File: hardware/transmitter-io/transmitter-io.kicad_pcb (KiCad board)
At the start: 2 copper layers, 68.6 x 53.3 mm, 20 parts, among them J1 Input

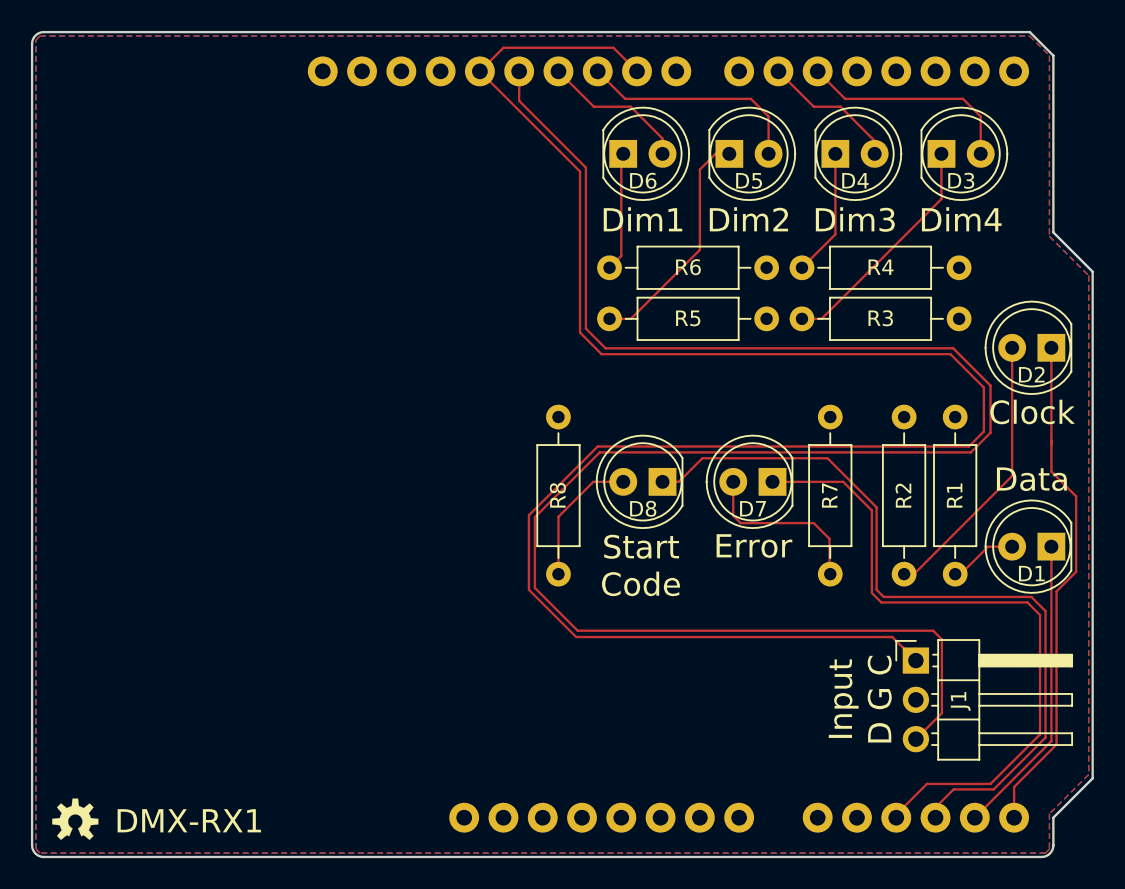
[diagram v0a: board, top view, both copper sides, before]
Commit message: Prototype version of DMX, Analog, and PWM IO Modules and both TX and RX IO interfaces.
Make io-analog a stackable family
io-analog-core handles D to A
io-analog-voltage handles voltage output
io-analog-pwm handles pwm output for leds, drive display pro

Refactor display-pro to work with io-analog-pwm
Add correct coax power connector

Move TX2 to tx-io
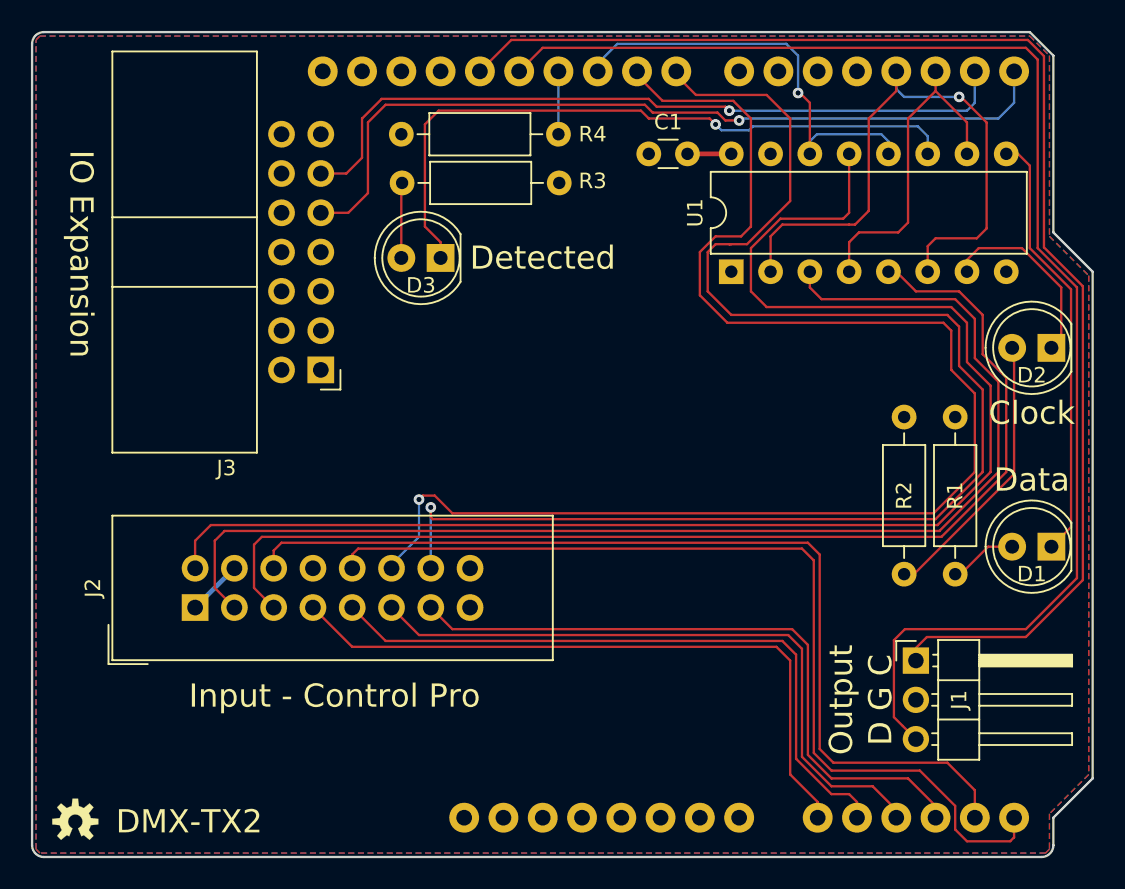
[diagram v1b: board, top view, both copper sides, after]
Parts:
- removed D4: DIM2, LED_THT:LED_D5.0mm
- removed D5: DIM1, LED_THT:LED_D5.0mm
- removed D6: DIM0, LED_THT:LED_D5.0mm
- removed D7: ERROR, LED_THT:LED_D5.0mm
- removed D8: START_CODE, LED_THT:LED_D5.0mm
- removed R5, R6, R7, R8: 330, Resistor_THT:R_Axial_DIN0207_L6.3mm_D2.5mm_P10.16mm_Horizontal
- added C1: 0.1uF, Capacitor_THT:C_Disc_D3.0mm_W1.6mm_P2.50mm, F.Cu at (156.2, 71.1)
- added J2: INPUT, Connector_IDC:IDC-Header_2x08_P2.54mm_Vertical, F.Cu at (126.9, 100.5)
- added J3: IO EXTENSION, Connector_IDC:IDC-Header_2x07_P2.54mm_Horizontal, F.Cu at (135.0, 85.1)
- added U1: 74LS365, Package_DIP:DIP-16_W7.62mm, F.Cu at (161.5, 78.7)
- D3: value DIM3 -> DETECTED
- J1: value Input -> Output
- moved D3 33.1 mm to (142.7, 77.9), turned to 180 degrees
- moved R3 27.3 mm to (150.4, 73.0)
- moved R4 27.3 mm to (150.4, 69.8)
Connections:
- A1 pad 10: Net-(A1-Pad10) -> /A1
- A1 pad 11: /~ERR -> /A2
- A1 pad 12: /~SC -> /A3
- A1 pad 13: /~DATA -> /A4
- A1 pad 14: /~CLOCK -> /A5
- A1 pad 17: Net-(A1-Pad17) -> /~DATA_OUT
- A1 pad 18: Net-(A1-Pad18) -> /~CLOCK_OUT
- A1 pad 20: /~DIM3 -> Net-(A1-Pad20)
- A1 pad 21: /~DIM2 -> Net-(A1-Pad21)
- A1 pad 23: Net-(A1-Pad23) -> /~CLK_FST
- A1 pad 24: /RXCLK -> /~CLK_SLO
- A1 pad 25: /~DIM1 -> /~HWD_DT_OUT
- A1 pad 26: /~DIM0 -> Net-(A1-Pad26)
- A1 pad 9: Net-(A1-Pad9) -> /A0
- D1 pad 1: /~DATA -> Net-(D1-Pad1)
- D2 pad 1: /~CLOCK -> Net-(D2-Pad1)
- D3 pad 2: /~DIM3 -> Net-(D3-Pad2)
- R3 pad 1: GND -> +5V
- R3 pad 2: Net-(D3-Pad1) -> Net-(D3-Pad2)
- R4 pad 1: GND -> Net-(A1-Pad26)
- R4 pad 2: Net-(D4-Pad1) -> GND
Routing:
- net /~HWD_DT: track 0.00 -> 94.3 mm
- net /~CLK_SLO: track 0.00 -> 92.3 mm, vias 0 -> 1
- net /~CLK_FST: track 0.00 -> 92.3 mm, vias 0 -> 1
- net /A5: track 0.00 -> 62.8 mm
- net /A4: track 0.00 -> 62.5 mm
- net /~DATA: track 19.6 -> 73.2 mm
- net Net-(A1-Pad15): track 0.00 -> 53.3 mm, vias 0 -> 1
- net /~SC: track 50.4 -> 0.00 mm
- net Net-(A1-Pad16): track 0.00 -> 48.3 mm, vias 0 -> 1
- net /~CLOCK: track 33.0 -> 80.4 mm
- net /~ERR: track 43.4 -> 0.00 mm
- net /A0: track 0.00 -> 43.2 mm
- net /A3: track 0.00 -> 42.9 mm
- net /A1: track 0.00 -> 42.8 mm
- net /A2: track 0.00 -> 42.7 mm
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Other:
- board text added: "DMX-TX2"
- board text added: "DMX-TX2, Rev 1.2 Crazy Giraffe Software"
- board text added: "Detected"
- board text added: "IO Expansion"
- board text added: "Input - Control Pro"
- board text added: "Output"
- board text removed: "DMX-RX1"
- board text removed: "DMX-RX1, Rev 1.3 Crazy Giraffe Software"
- board text removed: "Dim1"
- board text removed: "Dim2"
- board text removed: "Dim3"
- board text removed: "Dim4"
- board text removed: "Error"
- board text removed: "Input"
- board text removed: "Start Code"
